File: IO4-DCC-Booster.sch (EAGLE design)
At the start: 52 parts, among them CON6 I2C, J2 NCE, J3 NCE, J4 LNET, J6 TRACK, J7 IBT-2, J8 CTL-IBT-2, Q6 2N7002

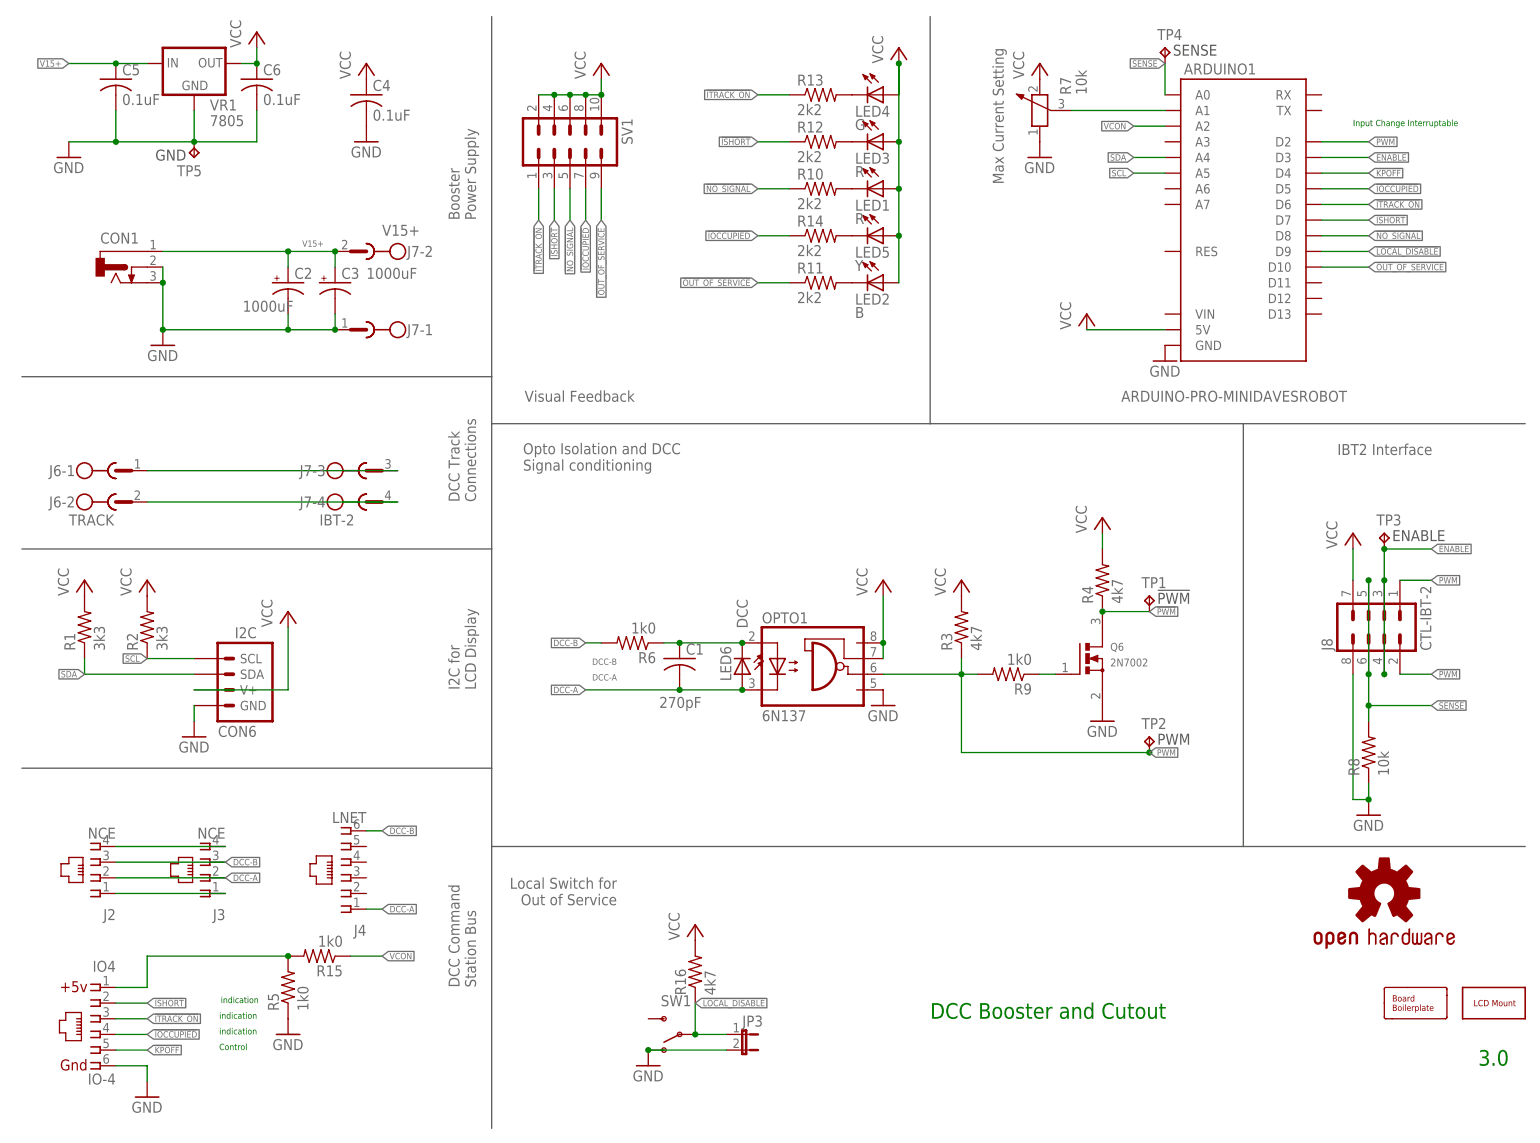
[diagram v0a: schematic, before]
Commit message: Rework, DC supply, simpler trace layout
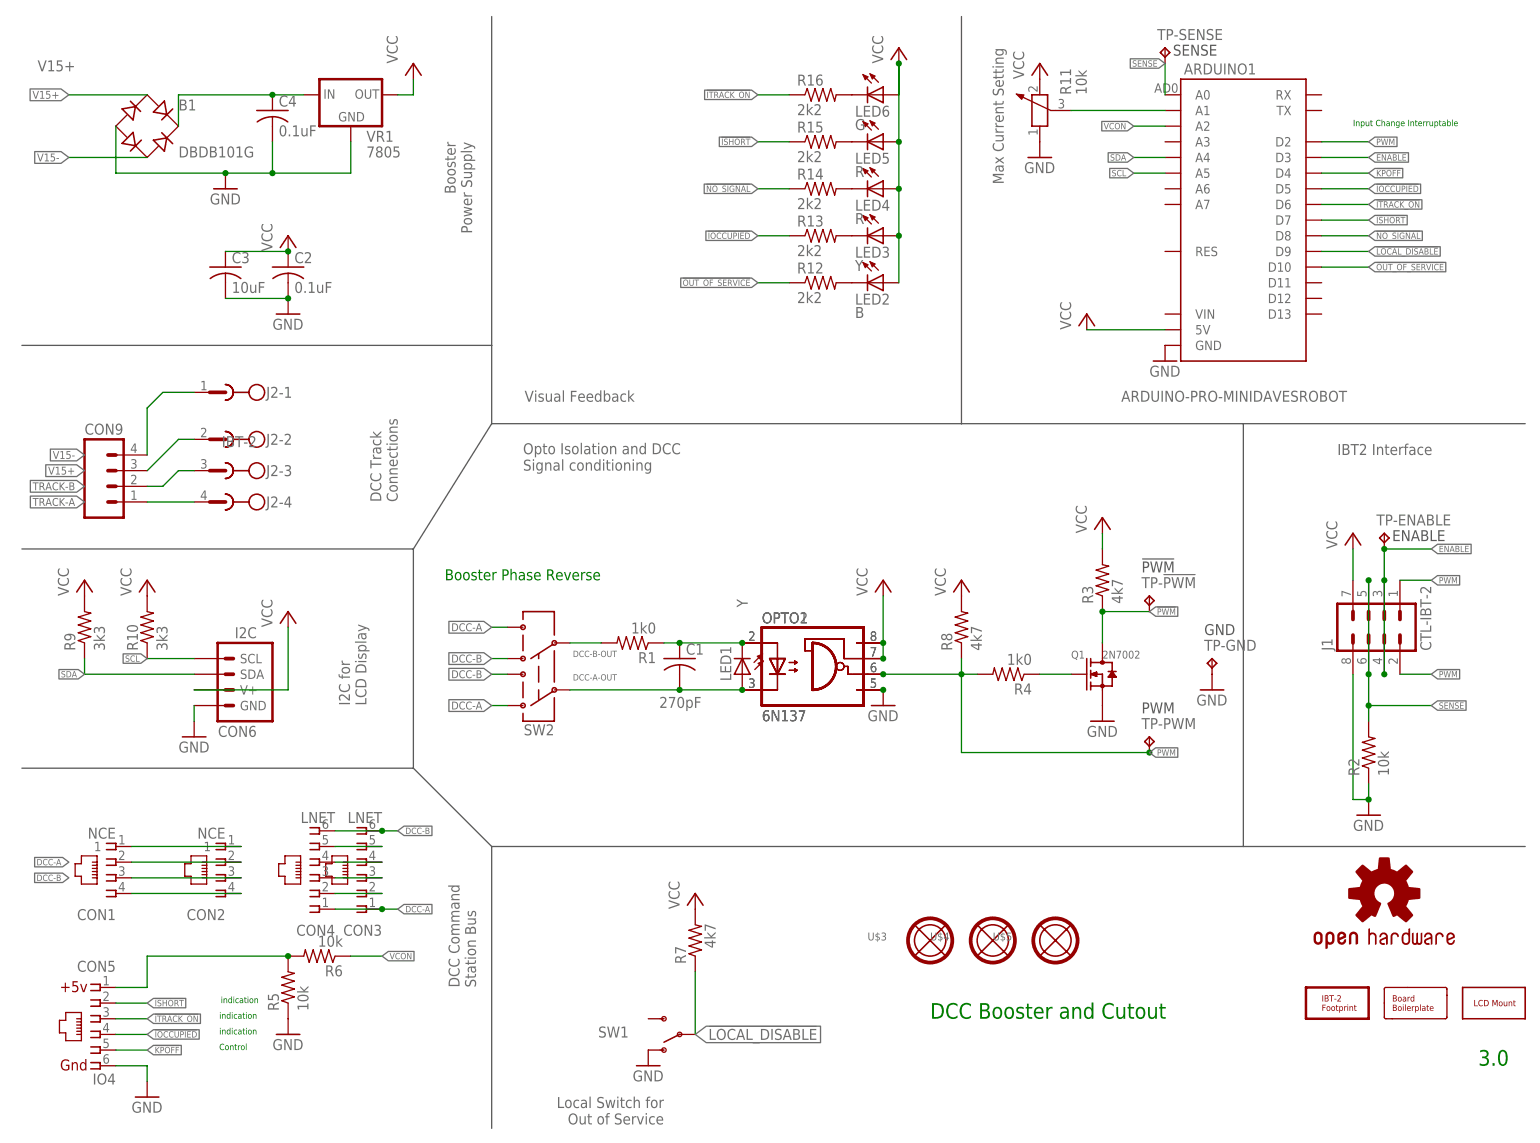
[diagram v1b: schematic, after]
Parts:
- removed C5, C6: 0.1uF, SPCoast:CAP0805
- removed IO4: IO-4, SPCoast:CONNECTOR-IO4INV
- removed J3: NCE, con-amp:555980-1
- removed J4: LNET, SPCoast:CONNECTOR-RJ25TOP
- removed J6: TRACK, con-phoenix-508:MSTBA2
- removed J7: IBT-2, con-phoenix-508:MSTBA4
- removed JP3: (no value), SPCoast:JUMPER-2PTH_LOCK
- removed Q6: 2N7002, microbuilder:MOSFET-NREFLOW
- removed SV1: (no value), con-lstb:MA05-2
- removed TP5: TPPAD1-13, testpad:TPPAD1-13
- added B1: DBDB101G, SPCoast:DBDB101G
- added CON2: NCE, SPCoast:CONNECTOR-RJ9-4P4C-AMP
- added CON3, CON4: LNET, SPCoast:CONNECTOR-RJ25-6P6C
- added CON5: IO4, SPCoast:CONNECTOR-IO4PNL
- added CON9: (no value), SPCoast:CONNECTOR-M045.08
- added OPTO2: 6N137, SPCoast:OPTO-6N137S
- added Q1: 2N7002, SPCoast:MOSFET-N-2N7002-SOT23
- added SW2: (no value), SPCoast:SWITCH-DPDTPTH-PB
- added TP-GND: TPPAD1-13, testpad:TPPAD1-13
- added U$2: IBT-2, SPCoast:IBT-2
- added U$3, U$4, U$5: MOUNTINGHOLE, SPCoast:MOUNTINGHOLE
- BOARD1: value (none) -> BOARD100X100-NOHOLES
- C2: value 1000uF -> 0.1uF; device SPCoast:CAP-POLPTH-5MM -> SPCoast:CAP0805
- C3: value 1000uF -> 10uF; device SPCoast:CAP-POLPTH-5MM -> SPCoast:CAP0805
- CON1: value (none) -> NCE; device SPCoast:CONNECTOR-DC-POWER-RA -> SPCoast:CONNECTOR-RJ9-4P4C-AMP
- J2: value NCE -> IBT-2; device con-amp:555980-1 -> con-phoenix-508:MSTBA4
- LED1, LED3: value R -> Y
- LED4: value G -> R
- LED5: value Y -> R
- LED6: value DCC -> G
- LOGO1: value DOC-OSHW-LOGOL -> DOC-OSHW-LOGO-L; device SPCoast:DOC-OSHW-LOGOL -> SPCoast:DOC-OSHW-LOGO-L
- R1: value 3k3 -> 1k0
- R10: value 2k2 -> 3k3
- R11: value 2k2 -> 10k; device SPCoast:R0805-RES -> SPCoast:R-POTENTIOMETERB25X
- R15: value 1k0 -> 2k2
- R16: value 4k7 -> 2k2
- R2: value 3k3 -> 10k
- R4: value 4k7 -> 1k0
- R5, R6: value 1k0 -> 10k
- R7: value 10k -> 4k7; device SPCoast:R-POTENTIOMETERB25X -> SPCoast:R0805-RES
- R8: value 10k -> 4k7
- R9: value 1k0 -> 3k3
- VR1: device SPCoast:VREG_78XXSIDE -> SPCoast:VREG-DPAK-5
- renumbered J8 to J1, TP1 to TP-!PWM, TP2 to TP-PWM, TP3 to TP-ENABLE, TP4 to TP-SENSE
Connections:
- removed net DCC+: J6-1.1, J7-3.1
- removed net DCC-: J6-2.1, J7-4.1
- removed net N$2: C1.1, LED6.C, OPTO1.A, R6.1
- removed net N$4: ARDUINO1.A1, R7.3
- new net DCC-A-OUT: C1.2, LED1.A, OPTO1.C, OPTO2.C, SW2.1C
- new net DCC-B-LIMITED: C1.1, LED1.C, OPTO1.A, OPTO2.A, R1.1
- new net DCC-B-OUT: R1.2, SW2.2C
- new net LIMIT: ARDUINO1.A1, R11.2
- new net N$11: CON3.3, CON4.3
- new net N$16: CON3.2, CON4.2
- new net N$19: B1.+, C4.1, VR1.IN
- new net N$8: CON3.5, CON4.5
- new net N$9: CON3.4, CON4.4
- new net TRACK-A: CON9.1, J2-4.1
- new net TRACK-B: CON9.2, J2-3.1
- new net V15-: B1.AC2, CON9.4, J2-1.1
- net !IOCCUPIED: now also CON5.4, R13.1; no longer IO4.4, R14.1, SV1.7
- net !ISHORT: now also CON5.2, R15.1; no longer IO4.2, R12.1, SV1.3
- net !ITRACK_ON: now also CON5.3, R16.1; no longer IO4.3, R13.1, SV1.1
- net !KPOFF: now also CON5.5; no longer IO4.5
- net !LOCAL_DISABLE: now also R7.1; no longer JP3.1, R16.1
- net !NO_SIGNAL: now also R14.1; no longer R10.1, SV1.5
- net !OUT_OF_SERVICE: now also R12.1; no longer R11.1, SV1.9
- net !PWM: now also Q1.D, R3.1; no longer Q6.D, R4.1
- net DCC-A: now also CON1.2, CON2.2, CON3.1, CON4.1, SW2.1A, SW2.2B; no longer C1.2, J2.2, J3.2, J4.1, LED6.A, OPTO1.C
- net DCC-B: now also CON1.3, CON2.3, CON3.6, CON4.6, SW2.1B, SW2.2A; no longer J2.3, J3.3, J4.6, R6.2
- net GND: now also B1.-, C2.2, C3.2, CON5.6, OPTO2.GND, Q1.S, R11.1, R2.1, TP-GND.TP; no longer C2.-, C3.-, C5.2, C6.2, CON1.2, CON1.3, IO4.6, J7-1.1, JP3.2, Q6.S, R7.1, R8.1, TP5.TP
- net N$1: now also Q1.G, R4.1; no longer Q6.G, R9.1
- net N$10: now also LED4.C, R14.2; no longer LED1.C, R10.2
- net N$12: now also R12.2; no longer R11.2
- net N$13: now also LED3.C, R13.2; no longer LED5.C, R14.2
- net N$14: now also LED6.C, R16.2; no longer LED4.C, R13.2
- net N$15: now also LED5.C, R15.2; no longer LED3.C, R12.2
- net N$6: now also CON1.4, CON2.4; no longer J2.4, J3.4
- net N$7: now also CON1.1, CON2.1; no longer J2.1, J3.1
- net PWM: now also OPTO2.VO, R4.2, R8.1; no longer R3.1, R9.2
- net SCL: now also R10.1; no longer R2.1
- net SDA: now also R9.1; no longer R1.1
- net SENSE: now also R2.2; no longer R8.2
- net V15+: now also B1.AC1, CON9.3, J2-2.1; no longer C2.+, C3.+, C5.1, CON1.1, J7-2.1, VR1.IN
- net VCC: now also C2.1, C3.1, LED6.A, OPTO2.VCC, OPTO2.VE, R10.2, R11.3, R8.2, R9.2; no longer C4.1, C6.1, LED1.A, R1.2, R16.2, R2.2, R4.2, SV1.10, SV1.2, SV1.4, SV1.6, SV1.8
- net VCOMPUTER: now also CON5.1, R6.2; no longer IO4.1, R15.2
- net VCON: now also R6.1; no longer R15.1
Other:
- note added: "Booster Phase Reverse"
- moved on the sheet: C4, LED1, LED3, LED4, LED5, LED6, R1, R10, R12, R13, R14, R15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

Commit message: normalized values
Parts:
- CON5: value IO4 -> RJ12/6
- CON9: value (none) -> 0.200
- J1: value CTL-IBT-2 -> 2x4-0.100
- LCD: value (none) -> LCD
- SW1: value (none) -> SPDT
- SW2: value (none) -> DPDT
- renumbered U$1 to LCD
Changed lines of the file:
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@@
 <grid distance="100" unitdist="mil" unit="mil" style="dots" multiple="1" display="yes" altdistance="50" altunitdist="mil" altunit="mil"/>
 <layers>
-<layer number="1" name="Top" color="4" fill="1" visible="yes" active="no"/>
-<layer number="2" name="Route2" color="1" fill="3" visible="yes" active="no"/>
-<layer number="3" name="Route3" color="4" fill="3" visible="yes" active="no"/>
-<layer number="14" name="Route14" color="1" fill="6" visible="yes" active="no"/>
-<layer number="15" name="Route15" color="4" fill="6" visible="yes" active="no"/>
-<layer number="16" name="Bottom" color="2" fill="1" visible="yes" active="no"/>
-<layer number="17" name="Pads" color="23" fill="1" visible="yes" active="no"/>
-<layer number="18" name="Vias" color="29" fill="1" visible="yes" active="no"/>
-<layer number="19" name="Unrouted" color="6" fill="1" visible="yes" active="no"/>
-<layer number="20" name="Dimension" color="15" fill="1" visible="yes" active="no"/>
-<layer number="21" name="tPlace" color="36" fill="1" visible="yes" active="no"/>
-<layer number="22" name="bPlace" color="17" fill="1" visible="yes" active="no"/>
-<layer number="23" name="tOrigins" color="30" fill="1" visible="yes" active="no"/>
-<layer number="24" name="bOrigins" color="15" fill="1" visible="yes" active="no"/>
-<layer number="25" name="tNames" color="63" fill="1" visible="yes" active="no"/>
-<layer number="26" name="bNames" color="34" fill="1" visible="yes" active="no"/>
-<layer number="27" name="tValues" color="56" fill="1" visible="yes" active="no"/>
-<layer number="28" name="bValues" color="7" fill="1" visible="yes" active="no"/>
+<layer number="1" name="Top" color="4" fill="1" visible="no" active="no"/>
+<layer number="2" name="Route2" color="1" fill="3" visible="no" active="no"/>
+<layer number="3" name="Route3" color="4" fill="3" visible="no" active="no"/>
+<layer number="14" name="Route14" color="1" fill="6" visible="no" active="no"/>
+<layer number="15" name="Route15" color="4" fill="6" visible="no" active="no"/>
+<layer number="16" name="Bottom" color="2" fill="1" visible="no" active="no"/>
+<layer number="17" name="Pads" color="23" fill="1" visible="no" active="no"/>
+<layer number="18" name="Vias" color="29" fill="1" visible="no" active="no"/>
+<layer number="19" name="Unrouted" color="6" fill="1" visible="no" active="no"/>
+<layer number="20" name="Dimension" color="15" fill="1" visible="no" active="no"/>
+<layer number="21" name="tPlace" color="36" fill="1" visible="no" active="no"/>
+<layer number="22" name="bPlace" color="17" fill="1" visible="no" active="no"/>
+<layer number="23" name="tOrigins" color="30" fill="1" visible="no" active="no"/>
+<layer number="24" name="bOrigins" color="15" fill="1" visible="no" active="no"/>
+<layer number="25" name="tNames" color="63" fill="1" visible="no" active="no"/>
+<layer number="26" name="bNames" color="34" fill="1" visible="no" active="no"/>
+<layer number="27" name="tValues" color="56" fill="1" visible="no" active="no"/>
+<layer number="28" name="bValues" color="7" fill="1" visible="no" active="no"/>
 <layer number="29" name="tStop" color="7" fill="3" visible="no" active="no"/>
 <layer number="30" name="bStop" color="7" fill="6" visible="no" active="no"/>
@@
 <layer number="35" name="tGlue" color="7" fill="4" visible="no" active="no"/>
 <layer number="36" name="bGlue" color="7" fill="5" visible="no" active="no"/>
-<layer number="37" name="tTest" color="7" fill="1" visible="yes" active="no"/>
-<layer number="38" name="bTest" color="7" fill="1" visible="yes" active="no"/>
+<layer number="37" name="tTest" color="7" fill="1" visible="no" active="no"/>
+<layer number="38" name="bTest" color="7" fill="1" visible="no" active="no"/>
 <layer number="39" name="tKeepout" color="4" fill="11" visible="no" active="no"/>
 <layer number="40" name="bKeepout" color="3" fill="11" visible="no" active="no"/>
@@
 <layer number="44" name="Drills" color="16" fill="1" visible="no" active="no"/>
 <layer number="45" name="Holes" color="35" fill="1" visible="no" active="no"/>
-<layer number="46" name="Milling" color="35" fill="1" visible="yes" active="no"/>
-<layer number="47" name="Measures" color="21" fill="1" visible="yes" active="no"/>
-<layer number="48" name="Document" color="36" fill="1" visible="yes" active="no"/>
-<layer number="49" name="Reference" color="48" fill="1" visible="yes" active="no"/>
-<layer number="50" name="dxf" color="7" fill="1" visible="yes" active="no"/>
-<layer number="51" name="tDocu" color="24" fill="1" visible="yes" active="no"/>
-<layer number="52" name="bDocu" color="7" fill="1" visible="yes" active="no"/>
-<layer number="53" name="tGND_GNDA" color="7" fill="9" visible="yes" active="no"/>
-<layer number="54" name="bGND_GNDA" color="1" fill="9" visible="yes" active="no"/>
-<layer number="56" name="wert" color="7" fill="1" visible="yes" active="no"/>
-<layer number="57" name="tCAD" color="7" fill="1" visible="yes" active="no"/>
-<layer number="59" name="tCarbon" color="7" fill="1" visible="yes" active="no"/>
-<layer number="60" name="bCarbon" color="7" fill="1" visible="yes" active="no"/>
+<layer number="46" name="Milling" color="35" fill="1" visible="no" active="no"/>
+<layer number="47" name="Measures" color="21" fill="1" visible="no" active="no"/>
+<layer number="48" name="Document" color="36" fill="1" visible="no" active="no"/>
+<layer number="49" name="Reference" color="48" fill="1" visible="no" active="no"/>
+<layer number="50" name="dxf" color="7" fill="1" visible="no" active="no"/>
+<layer number="51" name="tDocu" color="24" fill="1" visible="no" active="no"/>
+<layer number="52" name="bDocu" color="7" fill="1" visible="no" active="no"/>
+<layer number="53" name="tGND_GNDA" color="7" fill="9" visible="no" active="no"/>
+<layer number="54" name="bGND_GNDA" color="1" fill="9" visible="no" active="no"/>
+<layer number="56" name="wert" color="7" fill="1" visible="no" active="no"/>
+<layer number="57" name="tCAD" color="7" fill="1" visible="no" active="no"/>
+<layer number="59" name="tCarbon" color="7" fill="1" visible="no" active="no"/>
+<layer number="60" name="bCarbon" color="7" fill="1" visible="no" active="no"/>
 <layer number="90" name="Modules" color="5" fill="1" visible="yes" active="yes"/>
 <layer number="91" name="Nets" color="2" fill="1" visible="yes" active="yes"/>
@@
 <part name="FRAME1" library="SPCoast" deviceset="DOC-FRAME-LETTER" device=""/>
 <part name="ARDUINO1" library="SPCoast" deviceset="ARDUINO-PRO-MINI" device="DAVESROBOT"/>
-<part name="J1" library="con-lstb" deviceset="MA04-2" device="" value="CTL-IBT-2"/>
-<part name="CON5" library="SPCoast" deviceset="CONNECTOR-IO4" device="PNL" value="IO4"/>
+<part name="J1" library="con-lstb" deviceset="MA04-2" device="" value="2x4-0.100"/>
+<part name="CON5" library="SPCoast" deviceset="CONNECTOR-IO4" device="PNL" value="RJ12/6"/>
 <part name="GND1" library="supply1" deviceset="GND" device=""/>
 <part name="OPTO1" library="SPCoast" deviceset="OPTO-6N137" device="" value="6N137"/>
@@
 <part name="P+4" library="supply1" deviceset="VCC" device=""/>
 <part name="P+6" library="supply1" deviceset="VCC" device=""/>
-<part name="U$1" library="SPCoast" deviceset="LCD" device="1602"/>
+<part name="LCD" library="SPCoast" deviceset="LCD" device="1602" value="LCD"/>
 <part name="LED4" library="SPCoast" deviceset="LED*" device="0603-LED" value="R"/>
 <part name="LED2" library="SPCoast" deviceset="LED*" device="0603-LED" value="B"/>
@@
 <part name="R7" library="SPCoast" deviceset="R*" device="0805-RES" value="4k7"/>
 <part name="P+12" library="supply1" deviceset="VCC" device=""/>
-<part name="SW1" library="SPCoast" deviceset="SWITCH-SPST" device="PTH-508"/>
+<part name="SW1" library="SPCoast" deviceset="SWITCH-SPST" device="PTH-508" value="SPDT"/>
 <part name="TP-PWM" library="testpad" deviceset="TP" device="PAD1-13" value="TPPAD1-13">
 <attribute name="TP_SIGNAL_NAME" value="PWM"/>
@@
 <part name="U$4" library="SPCoast" deviceset="MOUNTINGHOLE" device=""/>
 <part name="U$5" library="SPCoast" deviceset="MOUNTINGHOLE" device=""/>
-<part name="SW2" library="SPCoast" deviceset="SWITCH-DPDT" device="PTH-PB"/>
-<part name="CON9" library="SPCoast" deviceset="CONNECTOR-M04" device="5.08"/>
+<part name="SW2" library="SPCoast" deviceset="SWITCH-DPDT" device="PTH-PB" value="DPDT"/>
+<part name="CON9" library="SPCoast" deviceset="CONNECTOR-M04" device="5.08" value="0.200"/>
 </parts>
 <sheets>
@@
 <attribute name="VALUE" x="152.4" y="88.9" size="1.778" layer="96" rot="R90"/>
 </instance>
-<instance part="U$1" gate="LCD" x="241.3" y="22.86" smashed="yes">
+<instance part="LCD" gate="LCD" x="241.3" y="22.86" smashed="yes">
 <attribute name="VALUE" x="237.236" y="20.574" size="1.778" layer="96"/>
 </instance>
